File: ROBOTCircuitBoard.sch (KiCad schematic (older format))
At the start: 13 parts, among them J1 DB15_HighDensity_MountingHoles, J2 DB15_HighDensity_MountingHoles, P1 CONN_01X03, P2 CONN_01X04, P3 CONN_01X04, P4 CONN_01X04, U1 MCP2551-I/P, U2 Teensy3.2

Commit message: Added four pin connectors, 5V layer, GND layer, and other misceallaneous jobs.
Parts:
- added P13, P15, P24, P?: CONN_01X04, Socket_Strips:Socket_Strip_Straight_1x04_Pitch2.54mm, symbol CONN_01X04
- added P5: CONN_01X05, Connectors_Terminal_Blocks:TerminalBlock_Pheonix_PT-3.5mm_5pol, symbol CONN_01X05
- P1: footprint Socket_Strips:Socket_Strip_Straight_1x03 -> Socket_Strips:Socket_Strip_Straight_1x03_Pitch2.54mm
- P2, P3, P4: footprint Socket_Strips:Socket_Strip_Straight_1x04 -> Socket_Strips:Socket_Strip_Straight_1x04_Pitch2.54mm
- U2: footprint Teensy:Teensy30_31_32_LC -> Teensy:Teensy30_31_32_LC_LessPins
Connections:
- net labels added: A0, A1, A2, A3, A6, A7, A8, A9
- wire segments 34 -> 58
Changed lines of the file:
@@
 LIBS:contrib
 LIBS:valves
-LIBS:teensy
 LIBS:ROBOTCircuitBoard-cache
 EELAYER 25 0
@@
 F 0 "U2" H 2950 6800 60  0000 C CNN
 F 1 "Teensy3.2" H 2950 3800 60  0000 C CNN
-F 2 "Teensy:Teensy30_31_32_LC" H 2950 4500 60  0001 C CNN
+F 2 "Teensy:Teensy30_31_32_LC_LessPins" H 2950 4500 60  0001 C CNN
 F 3 "" H 2950 4500 60  0000 C CNN
 	1    2950 5300
@@
 	0    1    1    0
 $EndComp
-Text Label 6200 2650 0    60   ~ 0
+Text Label 6200 2850 0    60   ~ 0
 CANL
-Text Label 6200 2850 0    60   ~ 0
-CANH
 $Comp
 L +5V #PWR07
@@
 F 0 "P1" H 5050 5250 50  0000 C CNN
 F 1 "CONN_01X03" V 5150 5050 50  0000 C CNN
-F 2 "Socket_Strips:Socket_Strip_Straight_1x03" H 5050 5050 50  0001 C CNN
+F 2 "Socket_Strips:Socket_Strip_Straight_1x03_Pitch2.54mm" H 5050 5050 50  0001 C CNN
 F 3 "" H 5050 5050 50  0000 C CNN
 	1    5050 5050
@@
 F 0 "P3" H 6800 5350 50  0000 C CNN
 F 1 "CONN_01X04" V 6900 5100 50  0000 C CNN
-F 2 "Socket_Strips:Socket_Strip_Straight_1x04" H 6800 5100 50  0001 C CNN
+F 2 "Socket_Strips:Socket_Strip_Straight_1x04_Pitch2.54mm" H 6800 5100 50  0001 C CNN
 F 3 "" H 6800 5100 50  0000 C CNN
 	1    6800 5100
@@
 F 0 "P4" H 6800 6150 50  0000 C CNN
 F 1 "CONN_01X04" V 6900 5900 50  0000 C CNN
-F 2 "Socket_Strips:Socket_Strip_Straight_1x04" H 6800 5900 50  0001 C CNN
+F 2 "Socket_Strips:Socket_Strip_Straight_1x04_Pitch2.54mm" H 6800 5900 50  0001 C CNN
 F 3 "" H 6800 5900 50  0000 C CNN
 	1    6800 5900
@@
 F 0 "P2" H 5850 4500 50  0000 C CNN
 F 1 "CONN_01X04" V 5950 4250 50  0000 C CNN
-F 2 "Socket_Strips:Socket_Strip_Straight_1x04" H 5850 4250 50  0001 C CNN
+F 2 "Socket_Strips:Socket_Strip_Straight_1x04_Pitch2.54mm" H 5850 4250 50  0001 C CNN
 F 3 "" H 5850 4250 50  0000 C CNN
 	1    5850 4250
@@
 	1    0    0    -1
 $EndComp
+Text Label 6200 2650 0    60   ~ 0
+CANH
+$Comp
+L CONN_01X04 P24
+U 1 1 58A8FC16
+P 9200 5900
+F 0 "P24" H 9200 6150 50  0000 C CNN
+F 1 "CONN_01X04" V 9300 5900 50  0000 C CNN
+F 2 "Socket_Strips:Socket_Strip_Straight_1x04_Pitch2.54mm" H 9200 5900 50  0001 C CNN
+F 3 "" H 9200 5900 50  0000 C CNN
+	1    9200 5900
+	1    0    0    -1
+$EndComp
+$Comp
+L CONN_01X04 P13
+U 1 1 58A8FC85
+P 8300 5800
+F 0 "P13" H 8300 6050 50  0000 C CNN
+F 1 "CONN_01X04" V 8400 5800 50  0000 C CNN
+F 2 "Socket_Strips:Socket_Strip_Straight_1x04_Pitch2.54mm" H 8300 5800 50  0001 C CNN
+F 3 "" H 8300 5800 50  0000 C CNN
+	1    8300 5800
+	1    0    0    -1
+$EndComp
+$Comp
+L CONN_01X04 P15
+U 1 1 58A8FDA2
+P 8300 5100
+F 0 "P15" H 8300 5350 50  0000 C CNN
+F 1 "CONN_01X04" V 8400 5100 50  0000 C CNN
+F 2 "Socket_Strips:Socket_Strip_Straight_1x04_Pitch2.54mm" H 8300 5100 50  0001 C CNN
+F 3 "" H 8300 5100 50  0000 C CNN
+	1    8300 5100
+	1    0    0    -1
+$EndComp
+$Comp
+L CONN_01X05 P5
+U 1 1 58AA31F6
+P 5050 5650
+F 0 "P5" H 5050 5950 50  0000 C CNN
+F 1 "CONN_01X05" V 5150 5650 50  0000 C CNN
+F 2 "Connectors_Terminal_Blocks:TerminalBlock_Pheonix_PT-3.5mm_5pol" H 5050 5650 50  0001 C CNN
+F 3 "" H 5050 5650 50  0000 C CNN
+	1    5050 5650
+	1    0    0    -1
+$EndComp
+Wire Wire Line
+	8100 4950 8000 4950
+Wire Wire Line
+	8100 5050 8000 5050
+Wire Wire Line
+	8100 5150 8000 5150
+Wire Wire Line
+	8100 5250 8000 5250
+Wire Wire Line
+	9000 5750 8900 5750
+Wire Wire Line
+	9000 5850 8900 5850
+Wire Wire Line
+	9000 5950 8900 5950
+Wire Wire Line
+	9000 6050 8900 6050
+Wire Wire Line
+	8100 5650 8000 5650
+Wire Wire Line
+	8100 5750 8000 5750
+Wire Wire Line
+	8100 5850 8000 5850
+Wire Wire Line
+	8100 5950 8000 5950
+Wire Wire Line
+	1950 6000 1800 6000
+Wire Wire Line
+	1950 6100 1800 6100
+Wire Wire Line
+	1950 6200 1800 6200
+Wire Wire Line
+	1950 6300 1800 6300
+Wire Wire Line
+	1950 6600 1800 6600
+Wire Wire Line
+	3950 6600 4100 6600
+Wire Wire Line
+	3950 6500 4100 6500
+Wire Wire Line
+	3950 6400 4100 6400
+$Comp
+L CONN_01X04 P?
+U 1 1 58AA511C
+P 9050 5150
+F 0 "P?" H 9050 5400 50  0000 C CNN
+F 1 "CONN_01X04" V 9150 5150 50  0000 C CNN
+F 2 "Socket_Strips:Socket_Strip_Straight_1x04_Pitch2.54mm" H 9050 5150 50  0001 C CNN
+F 3 "" H 9050 5150 50  0000 C CNN
+	1    9050 5150
+	1    0    0    -1
+$EndComp
+Wire Wire Line
+	8850 5000 8750 5000
+Wire Wire Line
+	8850 5100 8750 5100
+Wire Wire Line
+	8850 5200 8750 5200
+Wire Wire Line
+	8850 5300 8750 5300
+Text Label 8000 4950 0    60   ~ 0
+A0
+Text Label 8000 5050 0    60   ~ 0
+A1
+Text Label 8000 5650 0    60   ~ 0
+A2
+Text Label 8000 5750 0    60   ~ 0
+A3
+Text Label 8750 5000 0    60   ~ 0
+A6
+Text Label 8750 5100 0    60   ~ 0
+A7
+Text Label 8900 5750 0    60   ~ 0
+A8
+Text Label 8900 5850 0    60   ~ 0
+A9
+Text Label 1800 6000 0    60   ~ 0
+A0
 $EndSCHEMATC

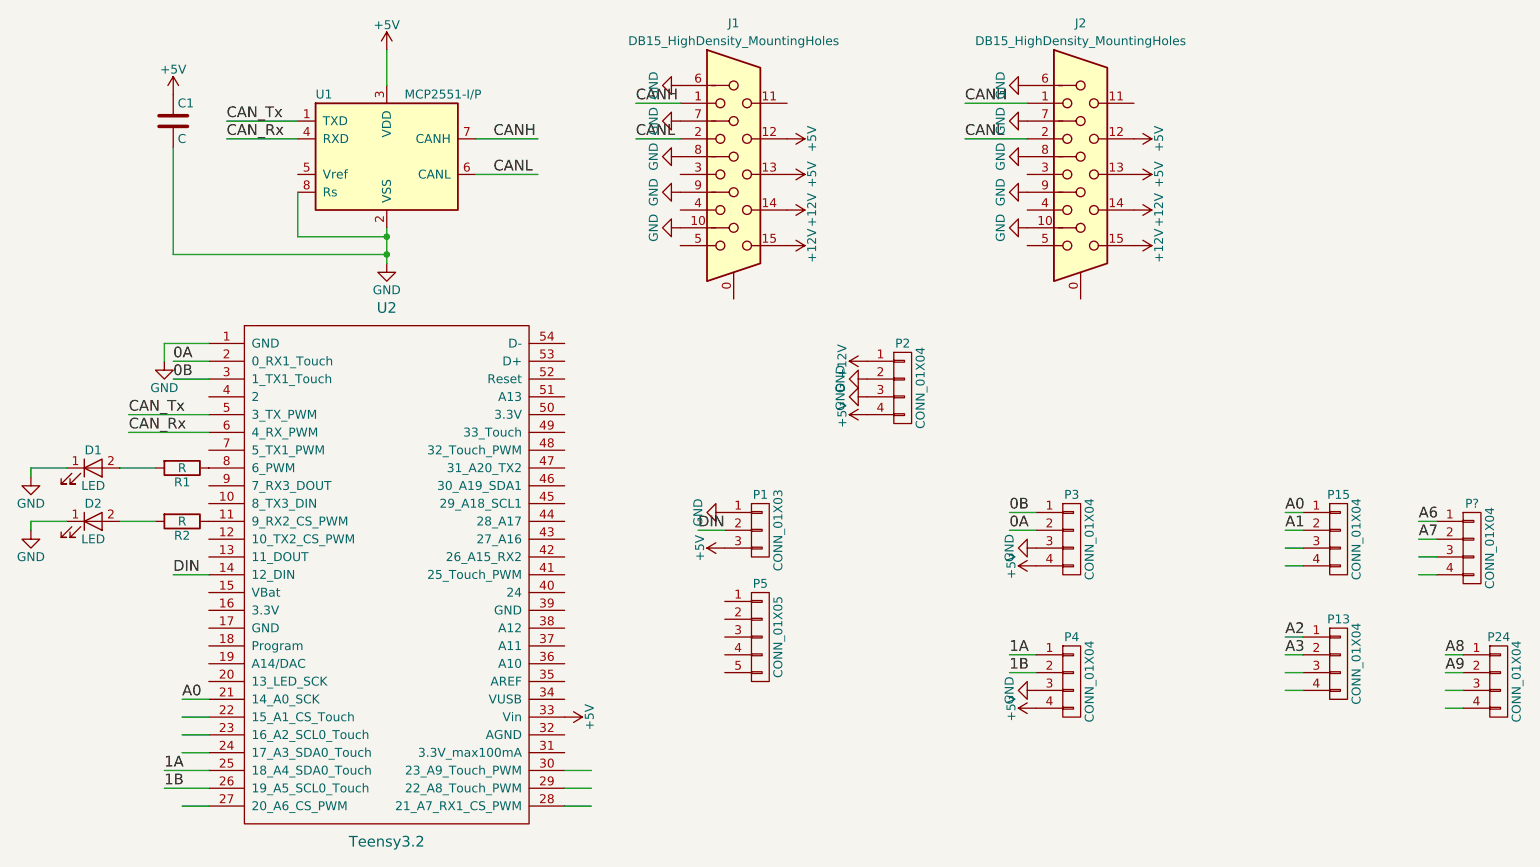
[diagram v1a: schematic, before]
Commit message: added some 5v GND DATA DATA ports. Repositioned Pololu. Reduced board size slightly
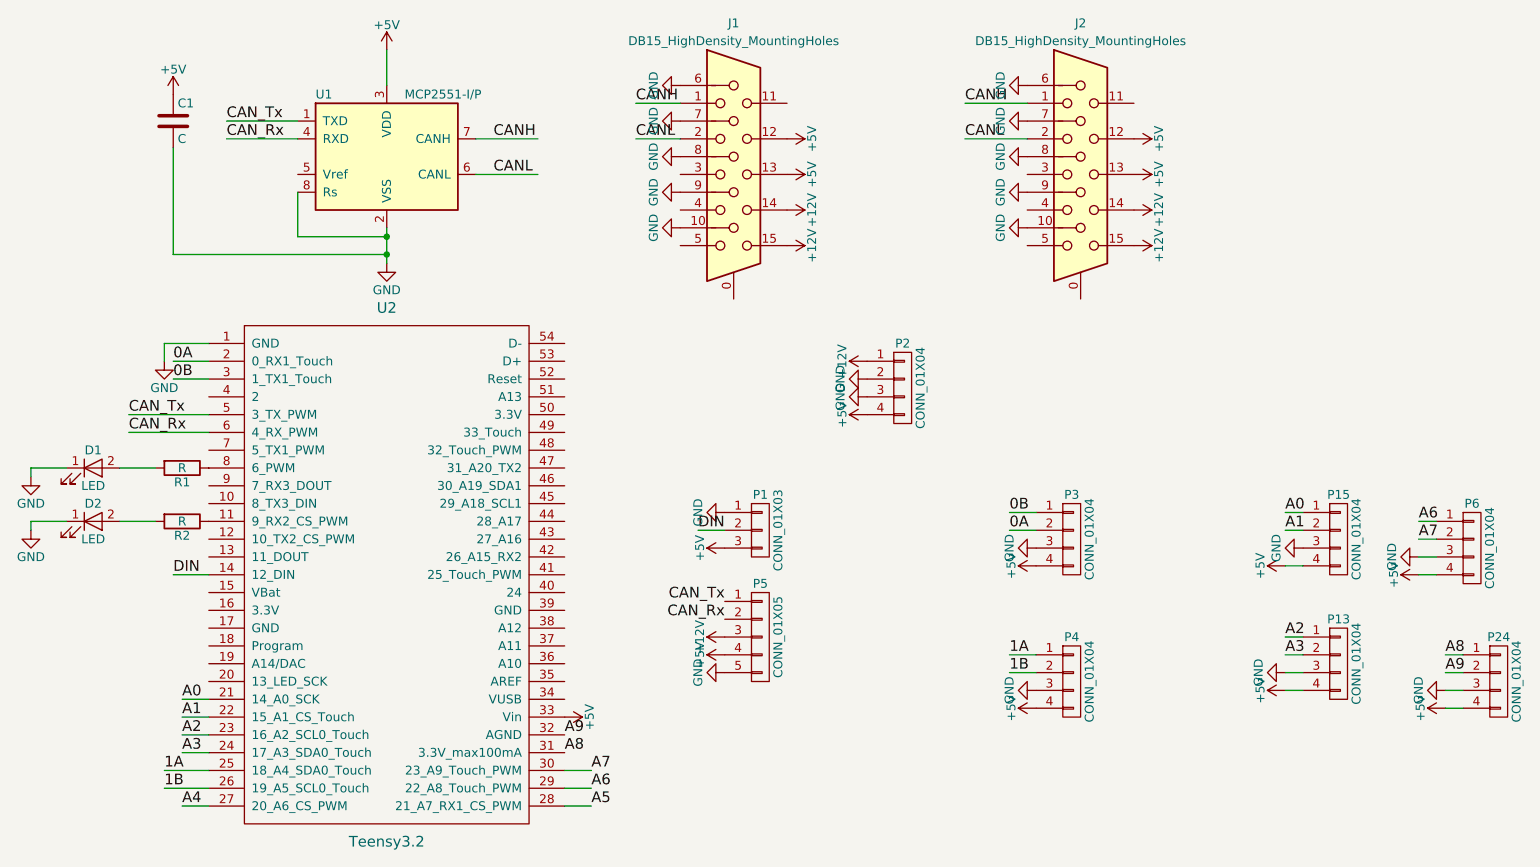
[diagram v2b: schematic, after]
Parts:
- gave numbers to parts that had none: 1
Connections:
- net labels added: A4, A5
- wire segments 58 -> 57
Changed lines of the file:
@@
 	8100 5050 8000 5050
 Wire Wire Line
-	8100 5150 8000 5150
-Wire Wire Line
 	8100 5250 8000 5250
 Wire Wire Line
@@
 	3950 6400 4100 6400
 $Comp
-L CONN_01X04 P?
+L CONN_01X04 P6
 U 1 1 58AA511C
 P 9050 5150
-F 0 "P?" H 9050 5400 50  0000 C CNN
+F 0 "P6" H 9050 5400 50  0000 C CNN
 F 1 "CONN_01X04" V 9150 5150 50  0000 C CNN
 F 2 "Socket_Strips:Socket_Strip_Straight_1x04_Pitch2.54mm" H 9050 5150 50  0001 C CNN
@@
 Text Label 1800 6000 0    60   ~ 0
 A0
+Text Label 1800 6100 0    60   ~ 0
+A1
+Text Label 1800 6200 0    60   ~ 0
+A2
+Text Label 1800 6300 0    60   ~ 0
+A3
+Text Label 1800 6600 0    60   ~ 0
+A4
+Text Label 4100 6600 0    60   ~ 0
+A5
+Text Label 4100 6500 0    60   ~ 0
+A6
+Text Label 4100 6400 0    60   ~ 0
+A7
+$Comp
+L GND #PWR036
+U 1 1 58AA51BB
+P 8000 5850
+F 0 "#PWR036" H 8000 5600 50  0001 C CNN
+F 1 "GND" H 8000 5700 50  0000 C CNN
+F 2 "" H 8000 5850 50  0000 C CNN
+F 3 "" H 8000 5850 50  0000 C CNN
+	1    8000 5850
+	0    1    1    0
+$EndComp
+$Comp
+L GND #PWR037
+U 1 1 58AA51FC
+P 8750 5200
+F 0 "#PWR037" H 8750 4950 50  0001 C CNN
+F 1 "GND" H 8750 5050 50  0000 C CNN
+F 2 "" H 8750 5200 50  0000 C CNN
+F 3 "" H 8750 5200 50  0000 C CNN
+	1    8750 5200
+	0    1    1    0
+$EndComp
+$Comp
+L GND #PWR038
+U 1 1 58AA52DC
+P 8100 5150
+F 0 "#PWR038" H 8100 4900 50  0001 C CNN
+F 1 "GND" H 8100 5000 50  0000 C CNN
+F 2 "" H 8100 5150 50  0000 C CNN
+F 3 "" H 8100 5150 50  0000 C CNN
+	1    8100 5150
+	0    1    1    0
+$EndComp
+$Comp
+L GND #PWR039
+U 1 1 58AA531D
+P 8900 5950
+F 0 "#PWR039" H 8900 5700 50  0001 C CNN
+F 1 "GND" H 8900 5800 50  0000 C CNN
+F 2 "" H 8900 5950 50  0000 C CNN
+F 3 "" H 8900 5950 50  0000 C CNN
+	1    8900 5950
+	0    1    1    0
+$EndComp
+$Comp
+L +5V #PWR040
+U 1 1 58AA5394
+P 8000 5950
+F 0 "#PWR040" H 8000 5800 50  0001 C CNN
+F 1 "+5V" H 8000 6090 50  0000 C CNN
+F 2 "" H 8000 5950 50  0000 C CNN
+F 3 "" H 8000 5950 50  0000 C CNN
+	1    8000 5950
+	0    -1   -1   0
+$EndComp
+$Comp
+L +5V #PWR041
+U 1 1 58AA53D5
+P 8000 5250
+F 0 "#PWR041" H 8000 5100 50  0001 C CNN
+F 1 "+5V" H 8000 5390 50  0000 C CNN
+F 2 "" H 8000 5250 50  0000 C CNN
+F 3 "" H 8000 5250 50  0000 C CNN
+	1    8000 5250
+	0    -1   -1   0
+$EndComp
+$Comp
+L +5V #PWR042
+U 1 1 58AA5416
+P 8750 5300
+F 0 "#PWR042" H 8750 5150 50  0001 C CNN
+F 1 "+5V" H 8750 5440 50  0000 C CNN
+F 2 "" H 8750 5300 50  0000 C CNN
+F 3 "" H 8750 5300 50  0000 C CNN
+	1    8750 5300
+	0    -1   -1   0
+$EndComp
+$Comp
+L +5V #PWR043
+U 1 1 58AA5457
+P 8900 6050
+F 0 "#PWR043" H 8900 5900 50  0001 C CNN
+F 1 "+5V" H 8900 6190 50  0000 C CNN
+F 2 "" H 8900 6050 50  0000 C CNN
+F 3 "" H 8900 6050 50  0000 C CNN
+	1    8900 6050
+	0    -1   -1   0
+$EndComp
+Text Label 4850 5450 2    60   ~ 0
+CAN_Tx
+Text Label 4850 5550 2    60   ~ 0
+CAN_Rx
+$Comp
+L +12V #PWR044
+U 1 1 58AA56E1
+P 4850 5650
+F 0 "#PWR044" H 4850 5500 50  0001 C CNN
+F 1 "+12V" H 4850 5790 50  0000 C CNN
+F 2 "" H 4850 5650 50  0000 C CNN
+F 3 "" H 4850 5650 50  0000 C CNN
+	1    4850 5650
+	0    -1   -1   0
+$EndComp
+$Comp
+L +5V #PWR045
+U 1 1 58AA576B
+P 4850 5750
+F 0 "#PWR045" H 4850 5600 50  0001 C CNN
+F 1 "+5V" H 4850 5890 50  0000 C CNN
+F 2 "" H 4850 5750 50  0000 C CNN
+F 3 "" H 4850 5750 50  0000 C CNN
+	1    4850 5750
+	0    -1   -1   0
+$EndComp
+$Comp
+L GND #PWR046
+U 1 1 58AA57B5
+P 4850 5850
+F 0 "#PWR046" H 4850 5600 50  0001 C CNN
+F 1 "GND" H 4850 5700 50  0000 C CNN
+F 2 "" H 4850 5850 50  0000 C CNN
+F 3 "" H 4850 5850 50  0000 C CNN
+	1    4850 5850
+	0    1    1    0
+$EndComp
+Text Label 3950 6300 0    60   ~ 0
+A8
+Text Label 3950 6200 0    60   ~ 0
+A9
 $EndSCHEMATC

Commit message: changed footprints and updated part number
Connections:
- net +5V: now also P13.3 (P3), P15.3 (P3), P24.3 (P3), P3.3 (P3), P4.3 (P3), P6.3 (P3); no longer P13.4 (P4), P15.4 (P4), P24.4 (P4), P3.4 (P4), P4.4 (P4), P6.4 (P4)
- net CANH: now also P5.2 (P2)
- net CANL: now also P5.1 (P1)
- net CAN_Rx: no longer P5.2 (P2)
- net CAN_Tx: no longer P5.1 (P1)
- net GND: now also P13.4 (P4), P15.4 (P4), P24.4 (P4), P3.4 (P4), P4.4 (P4), P6.4 (P4); no longer P13.3 (P3), P15.3 (P3), P24.3 (P3), P3.3 (P3), P4.3 (P3), P6.3 (P3)
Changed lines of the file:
@@
 Text Label 1500 4500 0    60   ~ 0
 CAN_Rx
-Text Label 3550 2850 0    60   ~ 0
+Text Label 3800 2850 0    60   ~ 0
 CANH
-Text Label 3550 3050 0    60   ~ 0
+Text Label 3800 3050 0    60   ~ 0
 CANL
 $Comp
@@
 L GND #PWR023
 U 1 1 587A6D4C
+P 6600 5250
+F 0 "#PWR023" H 6600 5000 50  0001 C CNN
+F 1 "GND" H 6600 5100 50  0000 C CNN
+F 2 "" H 6600 5250 50  0000 C CNN
+F 3 "" H 6600 5250 50  0000 C CNN
+	1    6600 5250
+	0    1    1    0
+$EndComp
+$Comp
+L +5V #PWR024
+U 1 1 587A6D81
 P 6600 5150
-F 0 "#PWR023" H 6600 4900 50  0001 C CNN
-F 1 "GND" H 6600 5000 50  0000 C CNN
+F 0 "#PWR024" H 6600 5000 50  0001 C CNN
+F 1 "+5V" H 6600 5290 50  0000 C CNN
 F 2 "" H 6600 5150 50  0000 C CNN
 F 3 "" H 6600 5150 50  0000 C CNN
 	1    6600 5150
-	0    1    1    0
-$EndComp
-$Comp
-L +5V #PWR024
-U 1 1 587A6D81
-P 6600 5250
-F 0 "#PWR024" H 6600 5100 50  0001 C CNN
-F 1 "+5V" H 6600 5390 50  0000 C CNN
-F 2 "" H 6600 5250 50  0000 C CNN
-F 3 "" H 6600 5250 50  0000 C CNN
-	1    6600 5250
 	0    -1   -1   0
 $EndComp
@@
 L +5V #PWR025
 U 1 1 587A706D
+P 6600 5950
+F 0 "#PWR025" H 6600 5800 50  0001 C CNN
+F 1 "+5V" H 6600 6090 50  0000 C CNN
+F 2 "" H 6600 5950 50  0000 C CNN
+F 3 "" H 6600 5950 50  0000 C CNN
+	1    6600 5950
+	0    -1   -1   0
+$EndComp
+$Comp
+L GND #PWR026
+U 1 1 587A70A2
 P 6600 6050
-F 0 "#PWR025" H 6600 5900 50  0001 C CNN
-F 1 "+5V" H 6600 6190 50  0000 C CNN
+F 0 "#PWR026" H 6600 5800 50  0001 C CNN
+F 1 "GND" H 6600 5900 50  0000 C CNN
 F 2 "" H 6600 6050 50  0000 C CNN
 F 3 "" H 6600 6050 50  0000 C CNN
 	1    6600 6050
-	0    -1   -1   0
-$EndComp
-$Comp
-L GND #PWR026
-U 1 1 587A70A2
-P 6600 5950
-F 0 "#PWR026" H 6600 5700 50  0001 C CNN
-F 1 "GND" H 6600 5800 50  0000 C CNN
-F 2 "" H 6600 5950 50  0000 C CNN
-F 3 "" H 6600 5950 50  0000 C CNN
-	1    6600 5950
 	0    1    1    0
 $EndComp
@@
 Wire Wire Line
 	8100 5050 8000 5050
-Wire Wire Line
-	8100 5250 8000 5250
 Wire Wire Line
 	9000 5750 8900 5750
@@
 L GND #PWR036
 U 1 1 58AA51BB
+P 8000 5950
+F 0 "#PWR036" H 8000 5700 50  0001 C CNN
+F 1 "GND" H 8000 5800 50  0000 C CNN
+F 2 "" H 8000 5950 50  0000 C CNN
+F 3 "" H 8000 5950 50  0000 C CNN
+	1    8000 5950
+	0    1    1    0
+$EndComp
+$Comp
+L GND #PWR037
+U 1 1 58AA51FC
+P 8750 5300
+F 0 "#PWR037" H 8750 5050 50  0001 C CNN
+F 1 "GND" H 8750 5150 50  0000 C CNN
+F 2 "" H 8750 5300 50  0000 C CNN
+F 3 "" H 8750 5300 50  0000 C CNN
+	1    8750 5300
+	0    1    1    0
+$EndComp
+$Comp
+L GND #PWR038
+U 1 1 58AA52DC
+P 8100 5250
+F 0 "#PWR038" H 8100 5000 50  0001 C CNN
+F 1 "GND" H 8100 5100 50  0000 C CNN
+F 2 "" H 8100 5250 50  0000 C CNN
+F 3 "" H 8100 5250 50  0000 C CNN
+	1    8100 5250
+	0    1    1    0
+$EndComp
+$Comp
+L GND #PWR039
+U 1 1 58AA531D
+P 8900 6050
+F 0 "#PWR039" H 8900 5800 50  0001 C CNN
+F 1 "GND" H 8900 5900 50  0000 C CNN
+F 2 "" H 8900 6050 50  0000 C CNN
+F 3 "" H 8900 6050 50  0000 C CNN
+	1    8900 6050
+	0    1    1    0
+$EndComp
+$Comp
+L +5V #PWR040
+U 1 1 58AA5394
 P 8000 5850
-F 0 "#PWR036" H 8000 5600 50  0001 C CNN
-F 1 "GND" H 8000 5700 50  0000 C CNN
+F 0 "#PWR040" H 8000 5700 50  0001 C CNN
+F 1 "+5V" H 8000 5990 50  0000 C CNN
 F 2 "" H 8000 5850 50  0000 C CNN
 F 3 "" H 8000 5850 50  0000 C CNN
 	1    8000 5850
-	0    1    1    0
-$EndComp
-$Comp
-L GND #PWR037
-U 1 1 58AA51FC
+	0    -1   -1   0
+$EndComp
+$Comp
+L +5V #PWR041
+U 1 1 58AA53D5
+P 8100 5150
+F 0 "#PWR041" H 8100 5000 50  0001 C CNN
+F 1 "+5V" H 8100 5290 50  0000 C CNN
+F 2 "" H 8100 5150 50  0000 C CNN
+F 3 "" H 8100 5150 50  0000 C CNN
+	1    8100 5150
+	0    -1   -1   0
+$EndComp
+$Comp
+L +5V #PWR042
+U 1 1 58AA5416
 P 8750 5200
-F 0 "#PWR037" H 8750 4950 50  0001 C CNN
-F 1 "GND" H 8750 5050 50  0000 C CNN
+F 0 "#PWR042" H 8750 5050 50  0001 C CNN
+F 1 "+5V" H 8750 5340 50  0000 C CNN
 F 2 "" H 8750 5200 50  0000 C CNN
 F 3 "" H 8750 5200 50  0000 C CNN
 	1    8750 5200
-	0    1    1    0
-$EndComp
-$Comp
-L GND #PWR038
-U 1 1 58AA52DC
-P 8100 5150
-F 0 "#PWR038" H 8100 4900 50  0001 C CNN
-F 1 "GND" H 8100 5000 50  0000 C CNN
-F 2 "" H 8100 5150 50  0000 C CNN
-F 3 "" H 8100 5150 50  0000 C CNN
-	1    8100 5150
-	0    1    1    0
-$EndComp
-$Comp
-L GND #PWR039
-U 1 1 58AA531D
+	0    -1   -1   0
+$EndComp
+$Comp
+L +5V #PWR043
+U 1 1 58AA5457
 P 8900 5950
-F 0 "#PWR039" H 8900 5700 50  0001 C CNN
-F 1 "GND" H 8900 5800 50  0000 C CNN
+F 0 "#PWR043" H 8900 5800 50  0001 C CNN
+F 1 "+5V" H 8900 6090 50  0000 C CNN
 F 2 "" H 8900 5950 50  0000 C CNN
 F 3 "" H 8900 5950 50  0000 C CNN
 	1    8900 5950
-	0    1    1    0
-$EndComp
-$Comp
-L +5V #PWR040
-U 1 1 58AA5394
-P 8000 5950
-F 0 "#PWR040" H 8000 5800 50  0001 C CNN
-F 1 "+5V" H 8000 6090 50  0000 C CNN
-F 2 "" H 8000 5950 50  0000 C CNN
-F 3 "" H 8000 5950 50  0000 C CNN
-	1    8000 5950
 	0    -1   -1   0
 $EndComp
-$Comp
-L +5V #PWR041
-U 1 1 58AA53D5
-P 8000 5250
-F 0 "#PWR041" H 8000 5100 50  0001 C CNN
-F 1 "+5V" H 8000 5390 50  0000 C CNN
-F 2 "" H 8000 5250 50  0000 C CNN
-F 3 "" H 8000 5250 50  0000 C CNN
-	1    8000 5250
-	0    -1   -1   0
-$EndComp
-$Comp
-L +5V #PWR042
-U 1 1 58AA5416
-P 8750 5300
-F 0 "#PWR042" H 8750 5150 50  0001 C CNN
-F 1 "+5V" H 8750 5440 50  0000 C CNN
-F 2 "" H 8750 5300 50  0000 C CNN
-F 3 "" H 8750 5300 50  0000 C CNN
-	1    8750 5300
-	0    -1   -1   0
-$EndComp
-$Comp
-L +5V #PWR043
-U 1 1 58AA5457
-P 8900 6050
-F 0 "#PWR043" H 8900 5900 50  0001 C CNN
-F 1 "+5V" H 8900 6190 50  0000 C CNN
-F 2 "" H 8900 6050 50  0000 C CNN
-F 3 "" H 8900 6050 50  0000 C CNN
-	1    8900 6050
-	0    -1   -1   0
-$EndComp
 Text Label 4850 5450 2    60   ~ 0
-CAN_Tx
+CANL
 Text Label 4850 5550 2    60   ~ 0
-CAN_Rx
+CANH
 $Comp
 L +12V #PWR044
